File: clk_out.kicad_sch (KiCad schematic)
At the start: 12 parts, among them U1001 74LVC1G157, U1002 74LVC2G04

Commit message: Update footprints: - SOD323F, SOD323, SOD123W... intead of generic handsolder version - 3225 xtal - use handsolder footprint - do not use handsolder version for ferrite beads - use SOT-23-6 instead of TSOP-6
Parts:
- D1001, D1002: footprint Diode_SMD:D_SOD-323_HandSoldering -> Diode_SMD:D_SOD-323F
- FB1001: footprint Inductor_SMD:L_0805_2012Metric_Pad1.05x1.20mm_HandSolder -> Inductor_SMD:L_0805_2012Metric
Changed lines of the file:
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@@
     (property "Reference" "FB1001" (id 0) (at 133.2992 45.7286 90))
     (property "Value" "782853701" (id 1) (at 133.2992 48.2655 90))
-    (property "Footprint" "Inductor_SMD:L_0805_2012Metric_Pad1.05x1.20mm_HandSolder" (id 2) (at 133.35 53.848 90)
+    (property "Footprint" "Inductor_SMD:L_0805_2012Metric" (id 2) (at 133.35 53.848 90)
       (effects (font (size 1.27 1.27)) hide)
     )
@@
       (effects (font (size 1.27 1.27)) (justify left))
     )
-    (property "Footprint" "Diode_SMD:D_SOD-323_HandSoldering" (id 2) (at 147.955 107.95 0)
+    (property "Footprint" "Diode_SMD:D_SOD-323F" (id 2) (at 147.955 107.95 0)
       (effects (font (size 1.27 1.27)) hide)
     )
@@
       (effects (font (size 1.27 1.27)) (justify left))
     )
-    (property "Footprint" "Diode_SMD:D_SOD-323_HandSoldering" (id 2) (at 146.685 95.25 0)
+    (property "Footprint" "Diode_SMD:D_SOD-323F" (id 2) (at 146.685 95.25 0)
       (effects (font (size 1.27 1.27)) hide)
     )

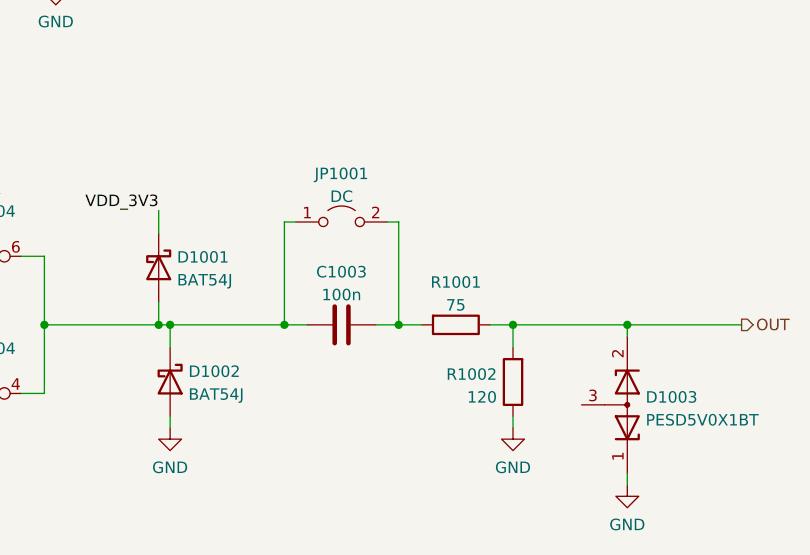
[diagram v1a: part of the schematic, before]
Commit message: Reconnect some things to simplify PCB routing
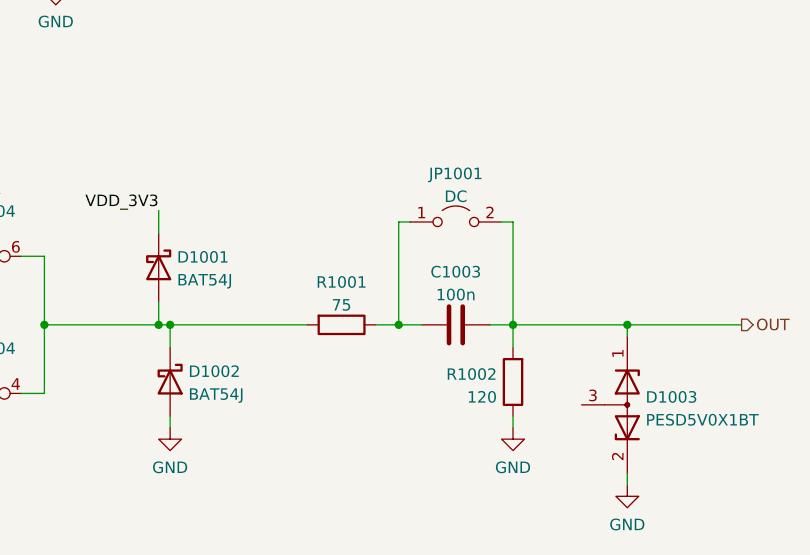
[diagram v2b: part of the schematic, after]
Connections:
- net GND: now also D1003.2 (K); no longer D1003.1 (K)
- net OUT: now also C1003.2, D1003.1 (K), JP1001.2 (B); no longer D1003.2 (K), R1001.1
- net at D1001.2 (A), D1002.1 (K), U1002.4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: now also R1001.2; no longer C1003.1, JP1001.1 (A)
- new net: C1003.1, JP1001.1 (A), R1001.1
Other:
- moved on the sheet: C1003, JP1001, R1001

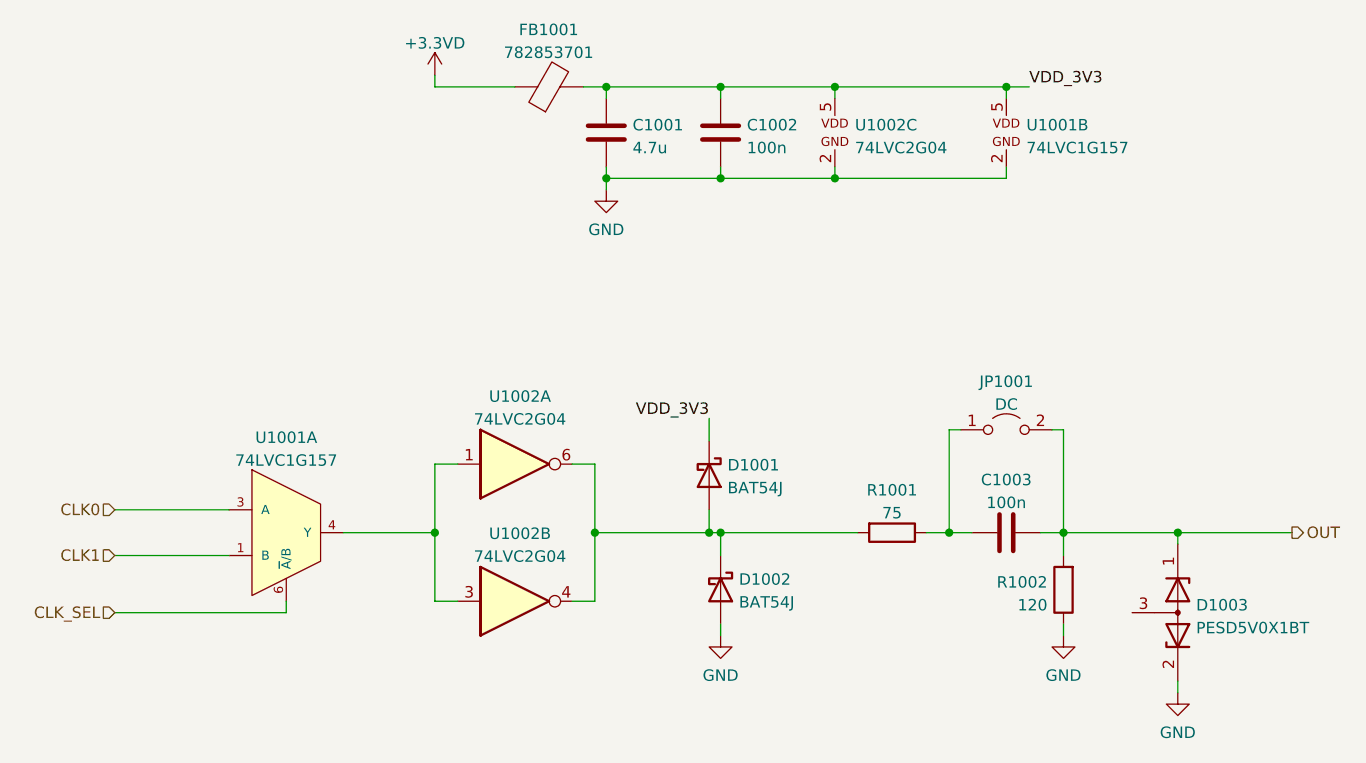
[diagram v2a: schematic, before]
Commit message: PCB: WIP Schematic: minor changes (decoupling, logic element ordering)
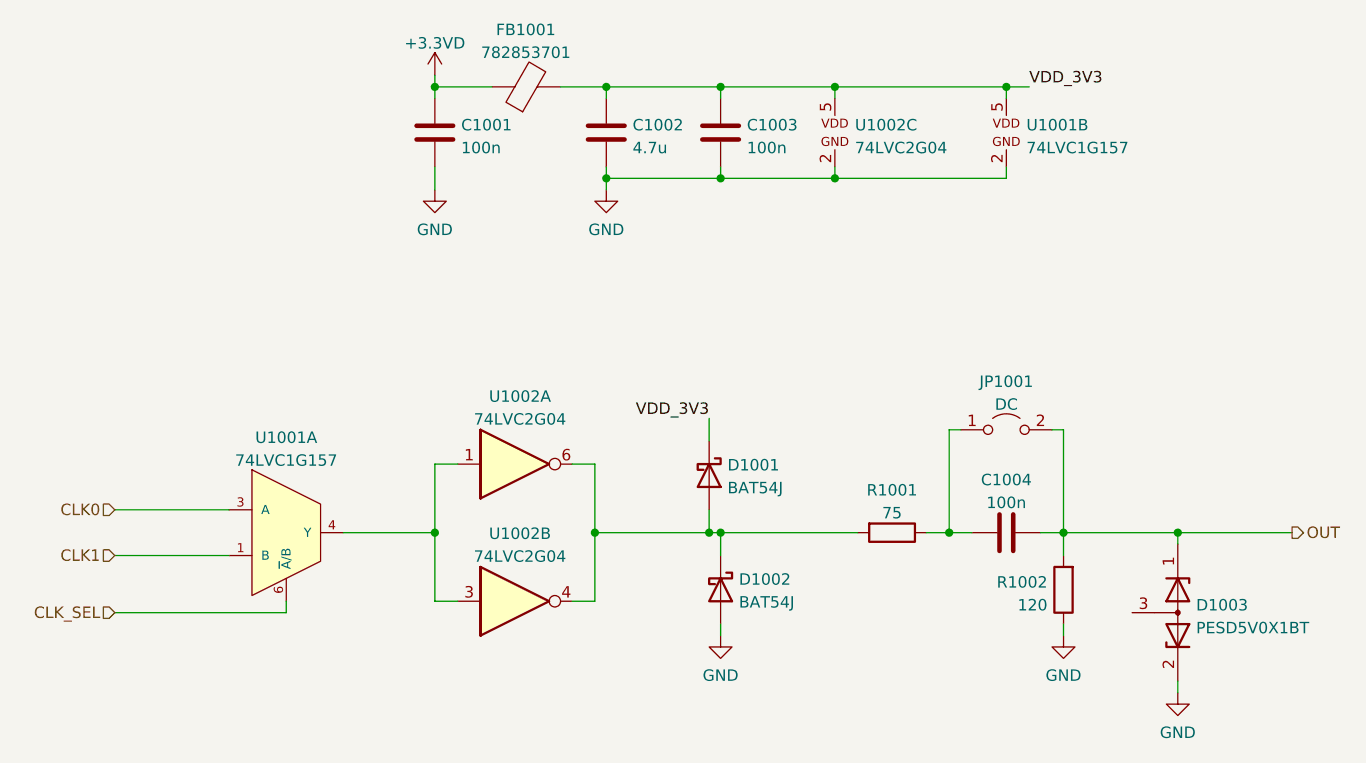
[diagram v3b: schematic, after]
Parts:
- added C1001: 100n, Capacitor_SMD:C_0805_2012Metric, symbol Device:C
- renumbered C1001 to C1002, C1002 to C1003, C1003 to C1004
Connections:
- net +3.3VD: now also C1001.2
- net GND: now also C1001.1
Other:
- moved on the sheet: FB1001

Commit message: Update schematic: - Redesign of decoupling based on swcad modelling (predominantly use 1uf, no paralleled caps) - Reroute REF_CLK_IN, CLK_SEL net to different FPGA pins - Some net renaming - Ext conn: add decoupling to 3v3 output - Reassign references to all components PCB: routing almost finished
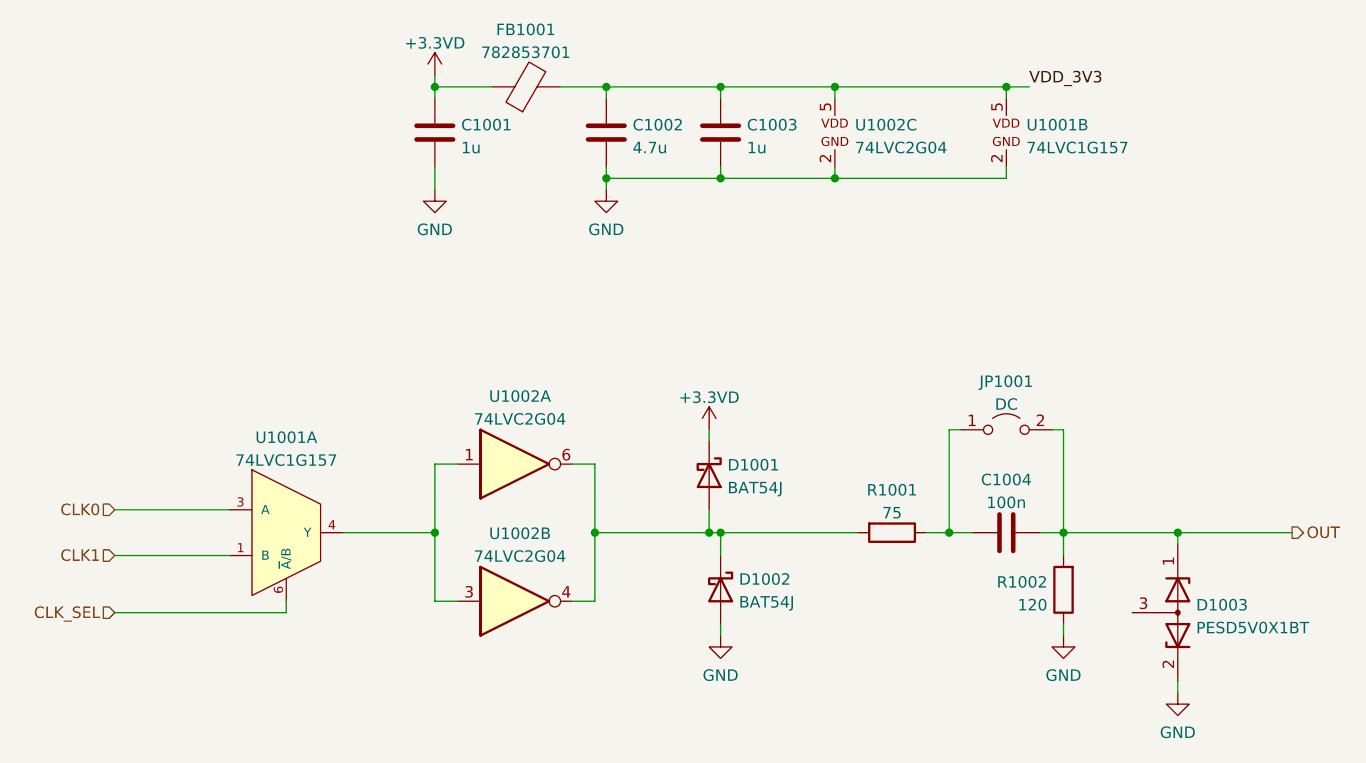
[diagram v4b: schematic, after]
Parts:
- C1001, C1003: value 100n -> 1u; Mfr PN CL21B104KBFNNNE -> CL21B105KOFNNNG
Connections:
- net +3.3VD: now also D1001.1 (K)
- net VDD_3V3: no longer D1001.1 (K)
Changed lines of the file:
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@@
     (stroke (width 0) (type default) (color 0 0 0 0))
   )
-  (wire (pts (xy 151.13 88.9) (xy 151.13 91.44))
+  (wire (pts (xy 151.13 90.17) (xy 151.13 91.44))
     (stroke (width 0) (type default) (color 0 0 0 0))
   )
@@
   (wire (pts (xy 175.26 101.6) (xy 177.8 101.6))
     (stroke (width 0) (type default) (color 0 0 0 0))
-  )
-  (label "VDD_3V3" (at 151.13 88.9 180)
-    (effects (font (size 1.27 1.27)) (justify right bottom))
   )
   (label "VDD_3V3" (at 186.69 52.07 0)
@@
     (pin "5")
   )
+  (symbol (lib_id "Device:C") (at 120.65 57.15 180) (unit 1)
+    (in_bom yes) (on_board yes) (fields_autoplaced)
+    (property "Reference" "C1001" (id 0) (at 123.571 56.3153 0)
+      (effects (font (size 1.27 1.27)) (justify right))
+    )
+    (property "Value" "1u" (id 1) (at 123.571 58.8522 0)
+      (effects (font (size 1.27 1.27)) (justify right))
+    )
+    (property "Footprint" "Capacitor_SMD:C_0805_2012Metric" (id 2) (at 119.6848 53.34 0)
+      (effects (font (size 1.27 1.27)) hide)
+    )
+    (property "Datasheet" "~" (id 3) (at 120.65 57.15 0)
+      (effects (font (size 1.27 1.27)) hide)
+    )
+    (property "Spec1" "" (id 4) (at 120.65 57.15 0)
+      (effects (font (size 1.27 1.27)) hide)
+    )
+    (property "Spec2" "" (id 5) (at 120.65 57.15 0)
+      (effects (font (size 1.27 1.27)) hide)
+    )
+    (property "Tolerance" "" (id 6) (at 120.65 57.15 0)
+      (effects (font (size 1.27 1.27)) hide)
+    )
+    (property "Mfr" "Samsung" (id 7) (at 120.65 57.15 0)
+      (effects (font (size 1.27 1.27)) hide)
+    )
+    (property "Mfr PN" "CL21B105KOFNNNG" (id 8) (at 120.65 57.15 0)
+      (effects (font (size 1.27 1.27)) hide)
+    )
+    (pin "1")
+    (pin "2")
+  )
   (symbol (lib_id "Device:R") (at 171.45 101.6 270) (unit 1)
     (in_bom yes) (on_board yes) (fields_autoplaced)
@@
   (symbol (lib_id "power:GND") (at 203.2 119.38 0) (unit 1)
     (in_bom yes) (on_board yes) (fields_autoplaced)
-    (property "Reference" "#PWR01006" (id 0) (at 203.2 125.73 0)
+    (property "Reference" "#PWR01007" (id 0) (at 203.2 125.73 0)
       (effects (font (size 1.27 1.27)) hide)
     )
@@
   (symbol (lib_id "power:GND") (at 190.5 113.03 0) (unit 1)
     (in_bom yes) (on_board yes) (fields_autoplaced)
-    (property "Reference" "#PWR01005" (id 0) (at 190.5 119.38 0)
+    (property "Reference" "#PWR01006" (id 0) (at 190.5 119.38 0)
       (effects (font (size 1.27 1.27)) hide)
     )
@@
     (pin "2")
   )
-  (symbol (lib_id "Device:C") (at 120.65 57.15 180) (unit 1)
-    (in_bom yes) (on_board yes) (fields_autoplaced)
-    (property "Reference" "C1001" (id 0) (at 123.571 56.3153 0)
+  (symbol (lib_id "symbols:+3.3VD") (at 151.13 90.17 0) (unit 1)
+    (in_bom yes) (on_board yes) (fields_autoplaced)
+    (property "Reference" "#PWR01004" (id 0) (at 151.13 93.98 0)
+      (effects (font (size 1.27 1.27)) hide)
+    )
+    (property "Value" "+3.3VD" (id 1) (at 151.13 86.5942 0))
+    (property "Footprint" "" (id 2) (at 151.13 90.17 0)
+      (effects (font (size 1.27 1.27)) hide)
+    )
+    (property "Datasheet" "" (id 3) (at 151.13 90.17 0)
+      (effects (font (size 1.27 1.27)) hide)
+    )
+    (pin "1")
+  )
+  (symbol (lib_id "Device:C") (at 152.4 57.15 180) (unit 1)
+    (in_bom yes) (on_board yes) (fields_autoplaced)
+    (property "Reference" "C1003" (id 0) (at 155.321 56.3153 0)
       (effects (font (size 1.27 1.27)) (justify right))
     )
-    (property "Value" "100n" (id 1) (at 123.571 58.8522 0)
+    (property "Value" "1u" (id 1) (at 155.321 58.8522 0)
       (effects (font (size 1.27 1.27)) (justify right))
     )
-    (property "Footprint" "Capacitor_SMD:C_0805_2012Metric" (id 2) (at 119.6848 53.34 0)
-      (effects (font (size 1.27 1.27)) hide)
-    )
-    (property "Datasheet" "~" (id 3) (at 120.65 57.15 0)
-      (effects (font (size 1.27 1.27)) hide)
-    )
-    (property "Spec1" "" (id 4) (at 120.65 57.15 0)
-      (effects (font (size 1.27 1.27)) hide)
-    )
-    (property "Spec2" "" (id 5) (at 120.65 57.15 0)
-      (effects (font (size 1.27 1.27)) hide)
-    )
-    (property "Tolerance" "" (id 6) (at 120.65 57.15 0)
-      (effects (font (size 1.27 1.27)) hide)
-    )
-    (property "Mfr" "Samsung" (id 7) (at 120.65 57.15 0)
-      (effects (font (size 1.27 1.27)) hide)
-    )
-    (property "Mfr PN" "CL21B104KBFNNNE" (id 8) (at 120.65 57.15 0)
+    (property "Footprint" "Capacitor_SMD:C_0805_2012Metric" (id 2) (at 151.4348 53.34 0)
+      (effects (font (size 1.27 1.27)) hide)
+    )
+    (property "Datasheet" "~" (id 3) (at 152.4 57.15 0)
+      (effects (font (size 1.27 1.27)) hide)
+    )
+    (property "Spec1" "" (id 4) (at 152.4 57.15 0)
+      (effects (font (size 1.27 1.27)) hide)
+    )
+    (property "Spec2" "" (id 5) (at 152.4 57.15 0)
+      (effects (font (size 1.27 1.27)) hide)
+    )
+    (property "Tolerance" "" (id 6) (at 152.4 57.15 0)
+      (effects (font (size 1.27 1.27)) hide)
+    )
+    (property "Mfr" "Samsung" (id 7) (at 152.4 57.15 0)
+      (effects (font (size 1.27 1.27)) hide)
+    )
+    (property "Mfr PN" "CL21B105KOFNNNG" (id 8) (at 152.4 57.15 0)
       (effects (font (size 1.27 1.27)) hide)
     )
@@
   (symbol (lib_id "power:GND") (at 152.4 113.03 0) (unit 1)
     (in_bom yes) (on_board yes) (fields_autoplaced)
-    (property "Reference" "#PWR01004" (id 0) (at 152.4 119.38 0)
+    (property "Reference" "#PWR01005" (id 0) (at 152.4 119.38 0)
       (effects (font (size 1.27 1.27)) hide)
     )
@@
       (effects (font (size 1.27 1.27)) hide)
     )
-    (pin "1")
-    (pin "2")
-  )
-  (symbol (lib_id "Device:C") (at 152.4 57.15 180) (unit 1)
-    (in_bom yes) (on_board yes) (fields_autoplaced)
-    (property "Reference" "C1003" (id 0) (at 155.321 56.3153 0)
-      (effects (font (size 1.27 1.27)) (justify right))
-    )
-    (property "Value" "100n" (id 1) (at 155.321 58.8522 0)
-      (effects (font (size 1.27 1.27)) (justify right))
-    )
-    (property "Footprint" "Capacitor_SMD:C_0805_2012Metric" (id 2) (at 151.4348 53.34 0)
-      (effects (font (size 1.27 1.27)) hide)
-    )
-    (property "Datasheet" "~" (id 3) (at 152.4 57.15 0)
-      (effects (font (size 1.27 1.27)) hide)
-    )
-    (property "Spec1" "" (id 4) (at 152.4 57.15 0)
-      (effects (font (size 1.27 1.27)) hide)
-    )
-    (property "Spec2" "" (id 5) (at 152.4 57.15 0)
-      (effects (font (size 1.27 1.27)) hide)
-    )
-    (property "Tolerance" "" (id 6) (at 152.4 57.15 0)
-      (effects (font (size 1.27 1.27)) hide)
-    )
-    (property "Mfr" "Samsung" (id 7) (at 152.4 57.15 0)
-      (effects (font (size 1.27 1.27)) hide)
-    )
-    (property "Mfr PN" "CL21B104KBFNNNE" (id 8) (at 152.4 57.15 0)
-      (effects (font (size 1.27 1.27)) hide)
-    )

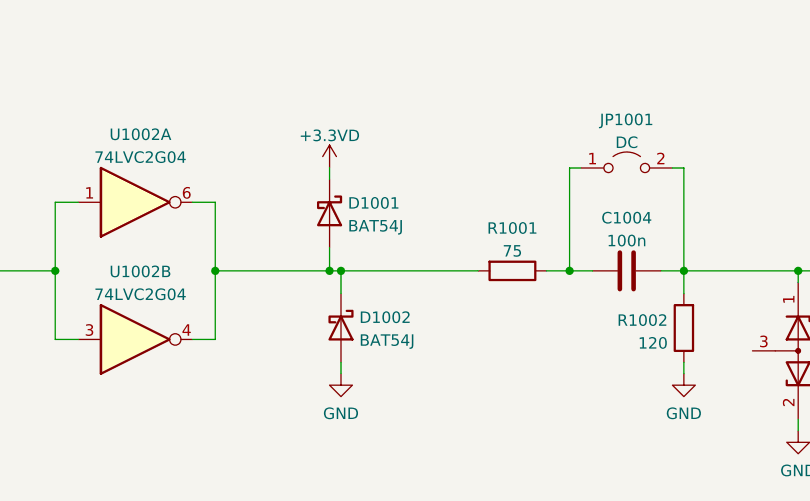
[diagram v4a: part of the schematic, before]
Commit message: Fix: correct BAT54 PN and package - SOD323 not SOD323F
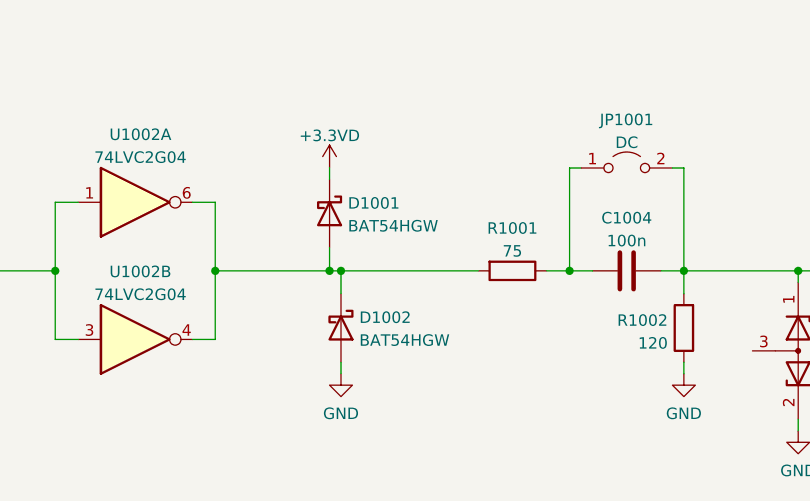
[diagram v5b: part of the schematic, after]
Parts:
- D1001, D1002: value BAT54J -> BAT54HGW; footprint Diode_SMD:D_SOD-323F -> Diode_SMD:D_SOD-323
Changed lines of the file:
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@@
       (effects (font (size 1.27 1.27)) (justify left))
     )
-    (property "Value" "BAT54J" (id 1) (at 154.432 109.3347 90)
+    (property "Value" "BAT54HGW" (id 1) (at 154.432 109.3347 90)
       (effects (font (size 1.27 1.27)) (justify left))
     )
-    (property "Footprint" "Diode_SMD:D_SOD-323F" (id 2) (at 147.955 107.95 0)
+    (property "Footprint" "Diode_SMD:D_SOD-323" (id 2) (at 147.955 107.95 0)
       (effects (font (size 1.27 1.27)) hide)
     )
@@
       (effects (font (size 1.27 1.27)) (justify left))
     )
-    (property "Value" "BAT54J" (id 1) (at 153.162 96.6347 90)
+    (property "Value" "BAT54HGW" (id 1) (at 153.162 96.6347 90)
       (effects (font (size 1.27 1.27)) (justify left))
     )
-    (property "Footprint" "Diode_SMD:D_SOD-323F" (id 2) (at 146.685 95.25 0)
+    (property "Footprint" "Diode_SMD:D_SOD-323" (id 2) (at 146.685 95.25 0)
       (effects (font (size 1.27 1.27)) hide)
     )
